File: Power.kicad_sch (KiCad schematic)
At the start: 29 parts, among them IC201 ADP2301AUJZ-R7, IC202 ADP2301AUJZ-R7, J201 AMASS_XT30PW-F, J202 AMASS_XT30PW-M, U201 LP5907QMFX-3.3Q1

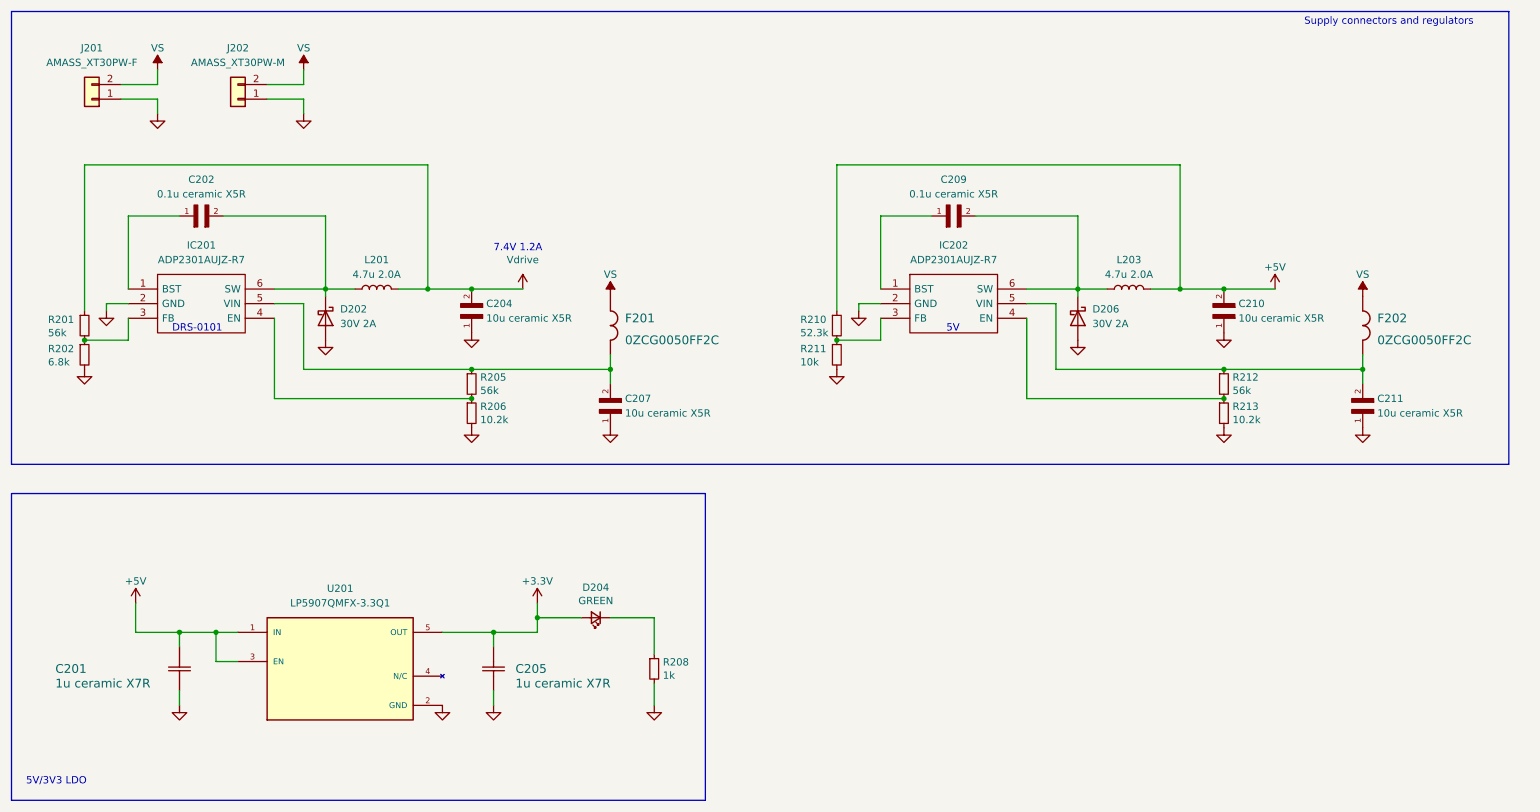
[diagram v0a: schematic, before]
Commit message: First draft routing
Separated into shield and main board projects
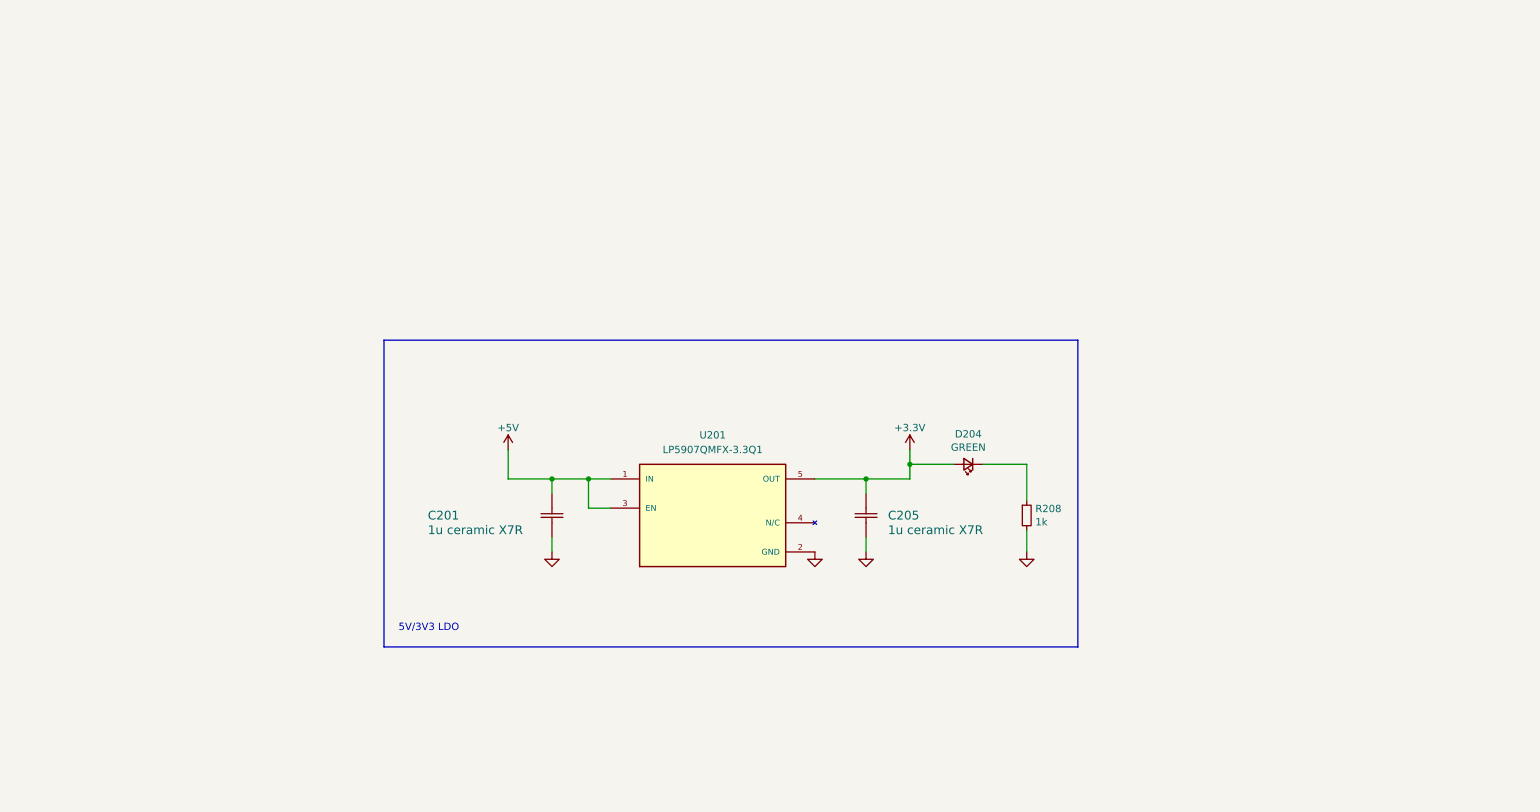
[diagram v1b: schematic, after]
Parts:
- removed C202, C209: 0.1u ceramic X5R, SnapEDA Library:CAPC1005X55N, symbol C1005X5R1E104K050BC:C1005X5R1E104K050BC
- removed C204, C207, C210, C211: 10u ceramic X5R, SnapEDA Library:CAPC1608X90N, symbol C1608X5R0J106K080AB:C1608X5R0J106K080AB
- removed D202, D206: 30V 2A, SnapEDA Library:B230A-13-F, symbol Device:D_Schottky
- removed F201, F202: 0ZCG0050FF2C, SnapEDA Library:0ZCG0050FF2C, symbol 0ZCG0050FF2C:0ZCG0050FF2C
- removed IC201, IC202: ADP2301AUJZ-R7, SOT95P280X100-6N, symbol ADP2301AUJZ-R7:ADP2301AUJZ-R7
- removed J201: AMASS_XT30PW-F, Connector_AMASS:AMASS_XT30PW-F_1x02_P2.50mm_Horizontal, symbol Connector_Generic:Conn_01x02
- removed J202: AMASS_XT30PW-M, Connector_AMASS:AMASS_XT30PW-M_1x02_P2.50mm_Horizontal, symbol Connector_Generic:Conn_01x02
- removed L201, L203: 4.7u 2.0A, SnapEDA Library:CDRH5D28RHPNP-4R7NC, symbol Device:L
- removed R201, R205, R212: 56k, Resistor_SMD:R_0402_1005Metric, symbol Device:R_Small
- removed R202: 6.8k, Resistor_SMD:R_0402_1005Metric, symbol Device:R_Small
- removed R206, R213: 10.2k, Resistor_SMD:R_0402_1005Metric, symbol Device:R_Small
- removed R210: 52.3k, Resistor_SMD:R_0402_1005Metric, symbol Device:R_Small
- removed R211: 10k, Resistor_SMD:R_0402_1005Metric, symbol Device:R_Small
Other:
- note removed: "5V"
- note removed: "7.4V 1.2A"
- note removed: "DRS-0101"
- note removed: "Supply connectors and regulators"
- moved on the sheet: C201, C205, D204, R208, U201
